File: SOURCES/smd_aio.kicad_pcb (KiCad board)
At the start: 2 copper layers, 159.8 x 99.8 mm, 225 parts, among them J1 RCA_01, J2 RCA_01, J3 RCA_01, J4 RCA_01, J5 Conn_01x02, J6 Conn_01x02, P1 MUTE, P10 CONN_01X02, P11 FCR684205T, P12 FCR684205R, P13 CONN_01X02, P14 CONN_01X02, P15 CONN_01X02, P16 TST, P17 MC4, P18 TST, P19 TST, P2 CONN_01X04, P20 TST, P21 TST, P22 TST, P23 TST, P24 MP11, P25 MP6, P26 MP10, P27 TST, P28 TST, P29 TST, P3 CONN_01X03, P30 TST, P31 CONN_01X03, P32 /SD, P33 GP4, P34 GP5, P35 GP6, P4 CONN_02X05 Boxed, P5 STDCONN, P6 CONN_02X04, P7 CONN_02X04, P8 CONN_02X04, P9 CONN_01X02, SW1 SW_PUSH, T1 Transformer_1P_1S_DA101JC, T2 Transformer_1P_1S_DA101JC, U1 ADAU1701, U10 IDT2309NZ, U11 LM1117MP-1.8, U12 LM1117MP-3.3, U13 OP279, U2 24AA256SN, U3 SN74LVC14ADG4, U4 TAS5760MDCAR, U5 CS8422-CNZ, U6 CS8406-CZZ, U7 LM2842Y, U8 MCP23008-xSS, U9 TAS5760MDCAR, X1 ASV-24.576MHz-EJ-T

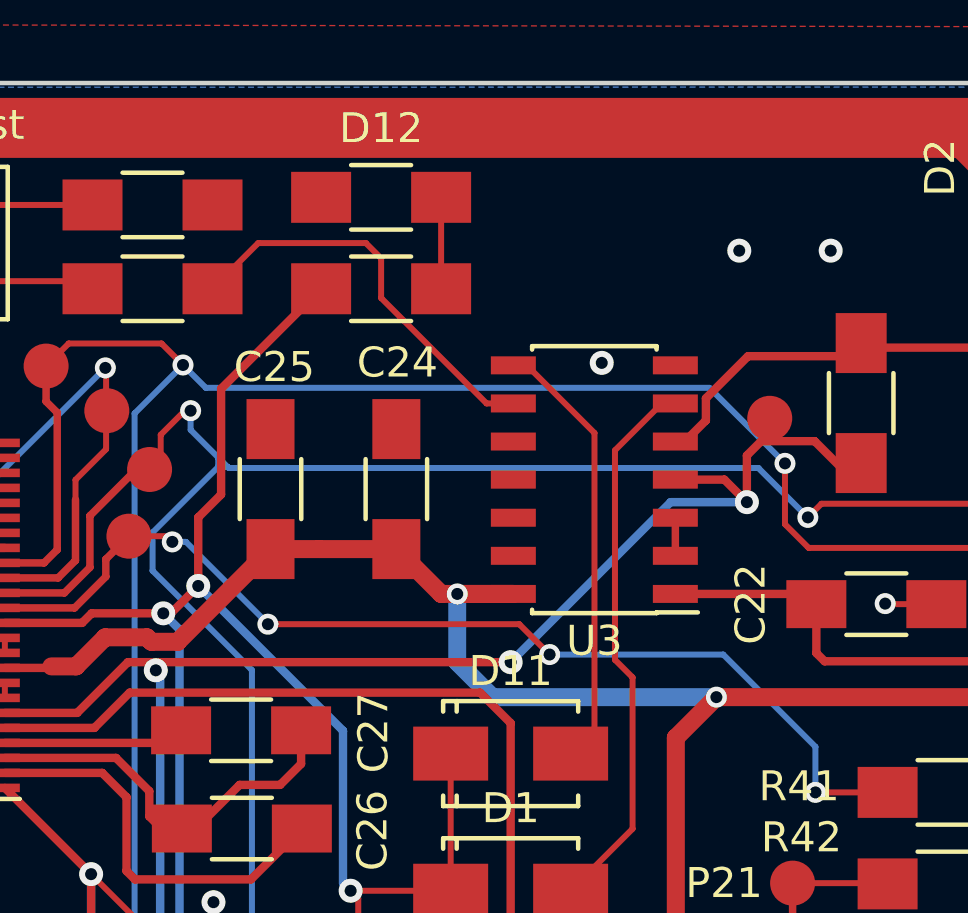
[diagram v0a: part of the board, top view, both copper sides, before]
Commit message: Added BAT54s OV protect.
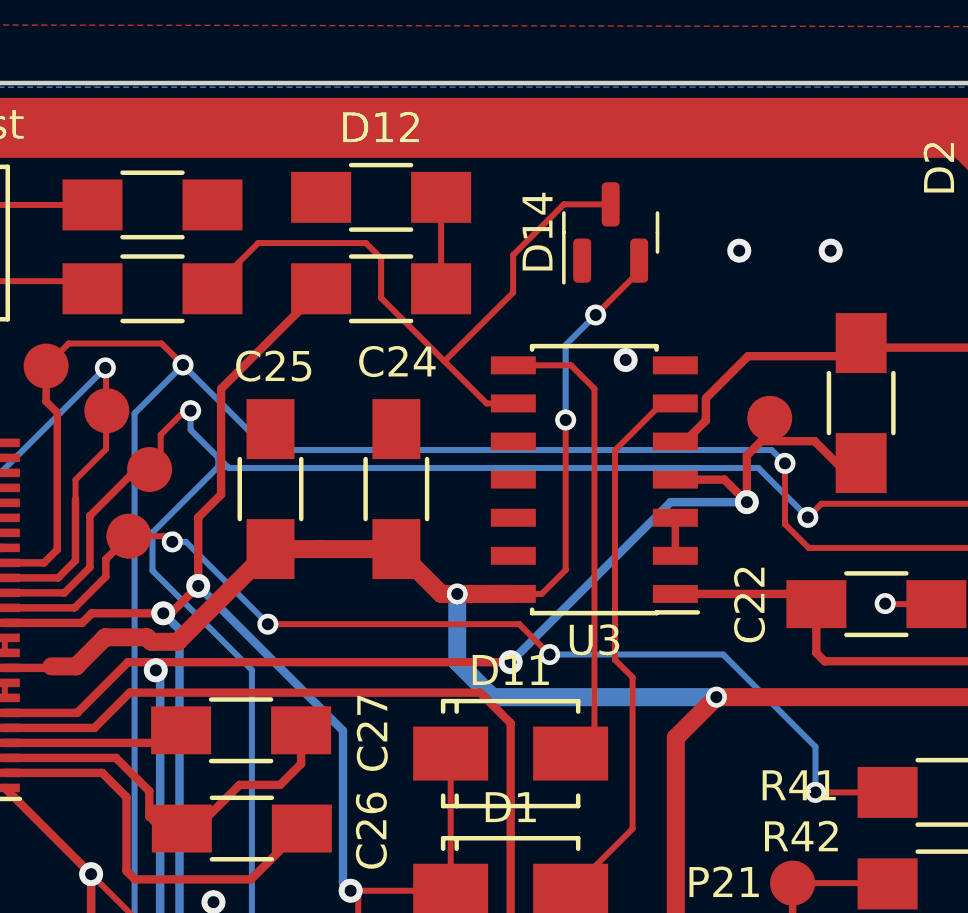
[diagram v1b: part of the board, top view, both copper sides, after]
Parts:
- added D14: BAT54S, Package_TO_SOT_SMD:SOT-23, F.Cu at (100.9, 22.0)
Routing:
- net +3V3: track 605.3 -> 618.7 mm, vias 14 -> 16
- net Net-(D14-COM): track 13.6 -> 22.1 mm
- net Net-(D11-A): track 14.7 -> 15.5 mm

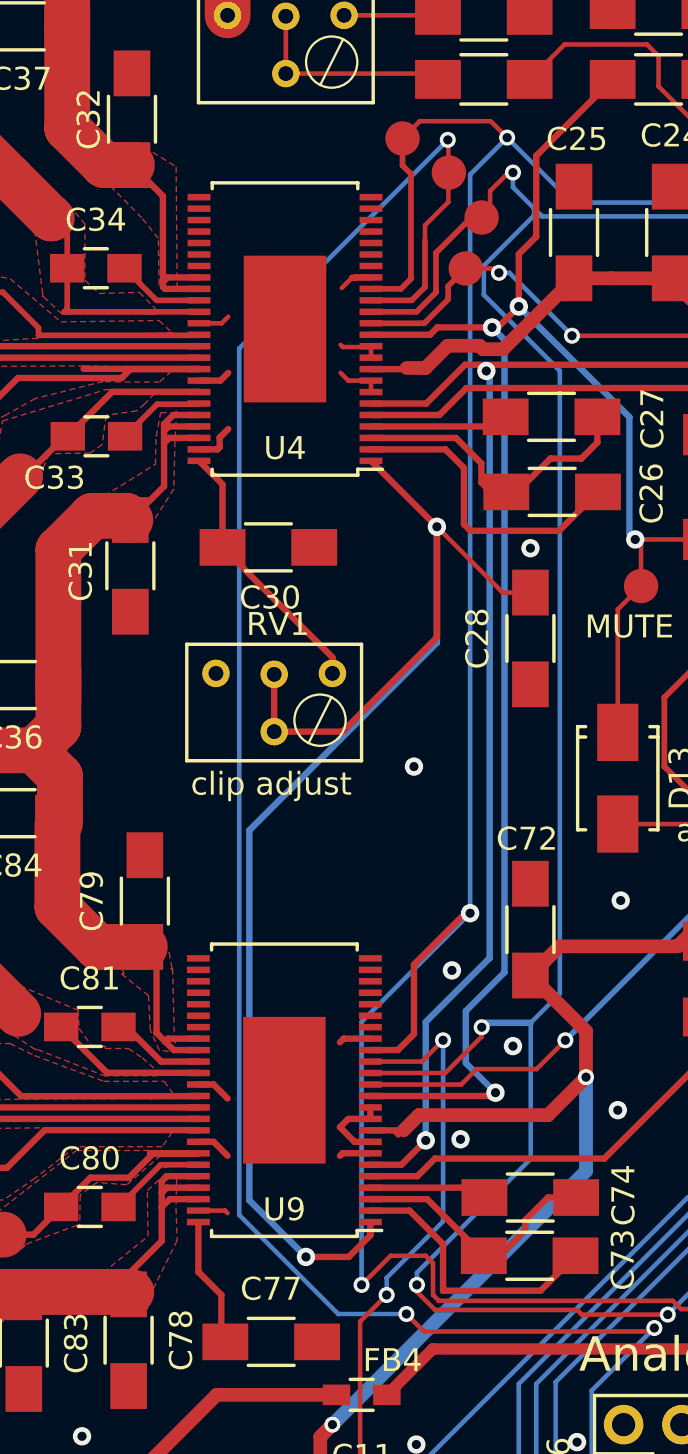
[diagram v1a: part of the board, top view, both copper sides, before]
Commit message: Cleaned up ground plane under amps.
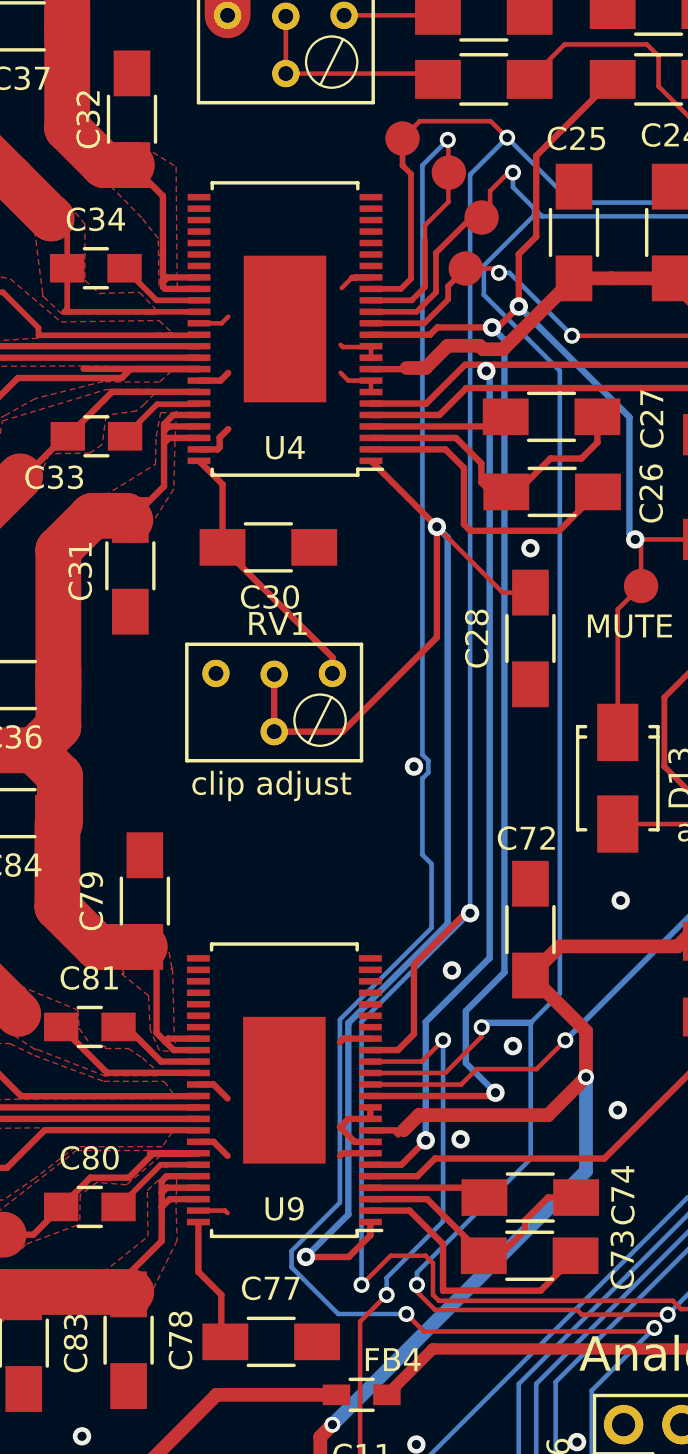
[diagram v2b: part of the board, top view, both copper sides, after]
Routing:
- net SFT_CLIP: track 65.5 -> 63.8 mm
- net MP6: track 110.7 -> 109.4 mm

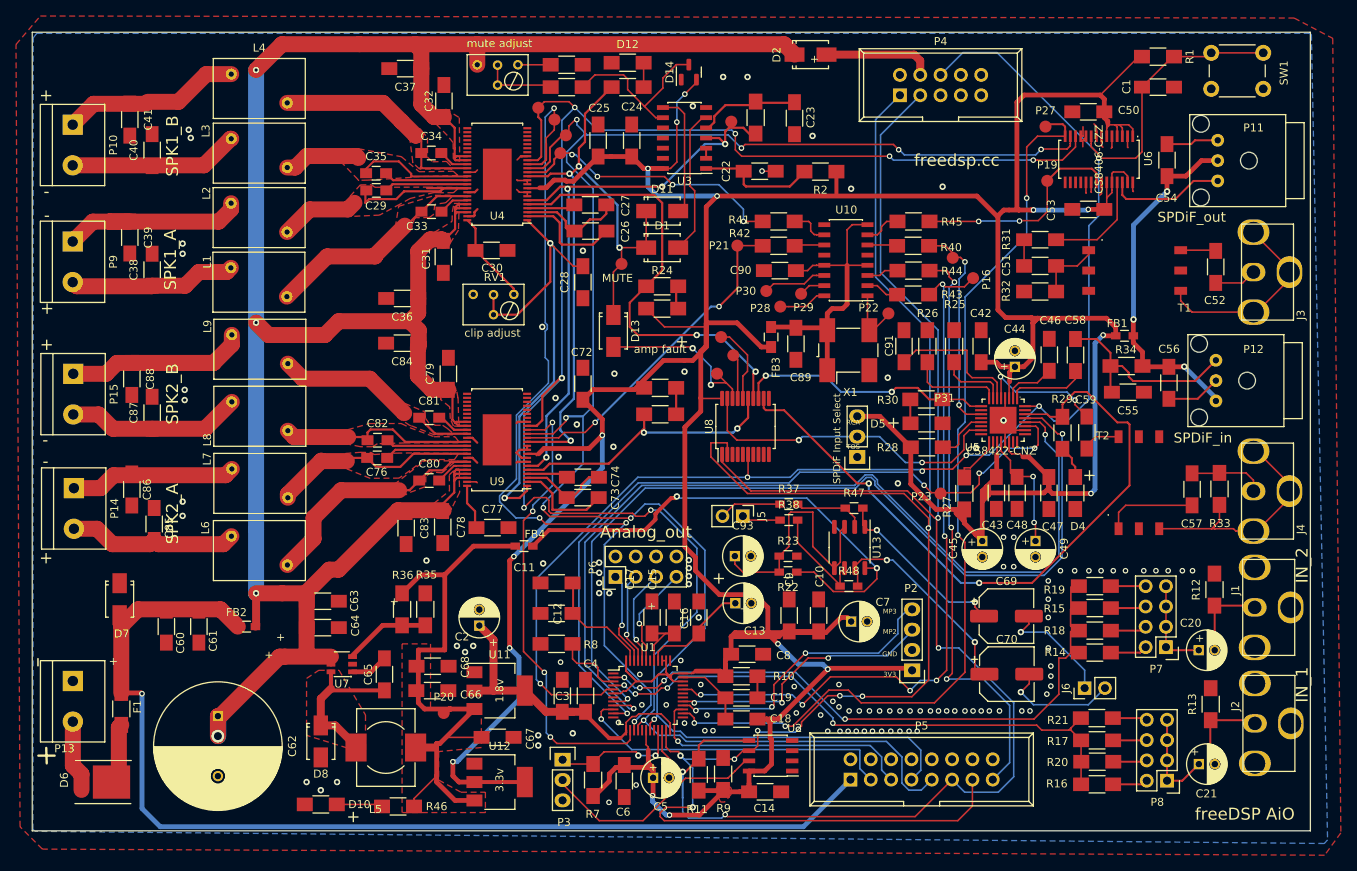
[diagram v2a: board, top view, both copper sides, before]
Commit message: Fixed Vin/Vcc issue.
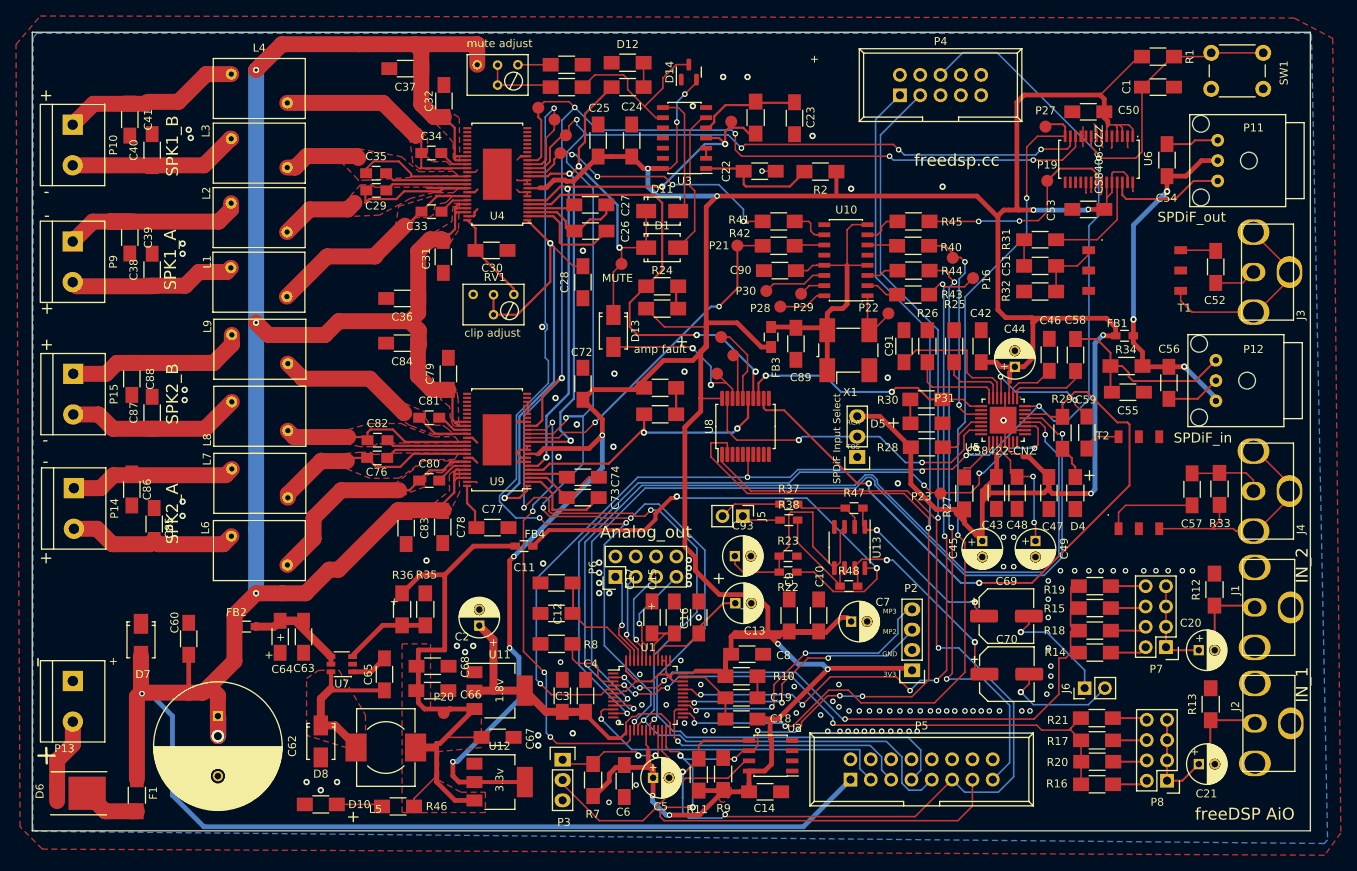
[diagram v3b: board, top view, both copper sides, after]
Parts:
- removed C61: 10u, fdsp_capacitor:C_1206_HandSoldering
- removed D2: B150, fdsp_diode:SMA
- moved F1 11.0 mm to (31.9, 112.4)
- moved D7 5.74 mm to (32.4, 93.0)
- moved C64 5.46 mm to (49.8, 92.6), turned to -90 degrees
- moved C63 5.06 mm to (52.7, 92.6), turned to -90 degrees
- moved D6 3.35 mm to (25.7, 112.1)
- moved C60 3.18 mm to (38.4, 92.8), turned to 90 degrees
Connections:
- C31 pad 1: VCC -> VIN
- C32 pad 1: VCC -> VIN
- C36 pad 1: VCC -> VIN
- C37 pad 1: VCC -> VIN
- C62 pad 1: VCC -> VIN
- C78 pad 1: VCC -> VIN
- C79 pad 1: VCC -> VIN
- C83 pad 1: VCC -> VIN
- C84 pad 1: VCC -> VIN
- RV2 pad 3: VCC -> VIN
- U4 pad 32: VCC -> VIN
- U4 pad 33: VCC -> VIN
- U4 pad 44: VCC -> VIN
- U4 pad 45: VCC -> VIN
- U4 pad 46: VCC -> VIN
- U9 pad 32: VCC -> VIN
- U9 pad 33: VCC -> VIN
- U9 pad 44: VCC -> VIN
- U9 pad 45: VCC -> VIN
- U9 pad 46: VCC -> VIN
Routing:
- net VCC: track 293.7 -> 15.6 mm, vias 4 -> 0
- net VIN: track 133.6 -> 375.7 mm, vias 1 -> 5
- net Net-(P4-P4): track 13.8 -> 0.00 mm
- net +12V: track 8.99 -> 10.8 mm

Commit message: Improved power traces.
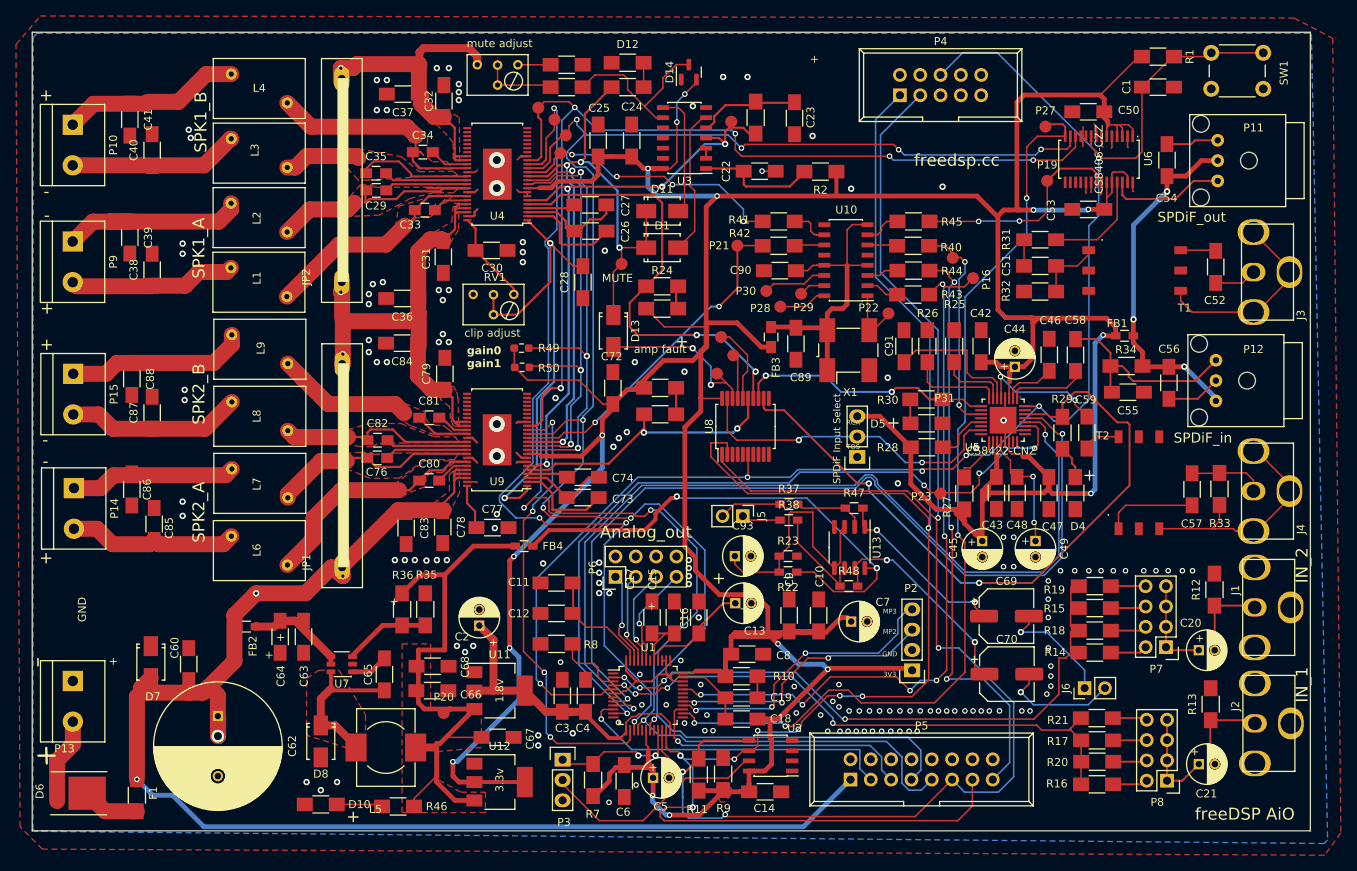
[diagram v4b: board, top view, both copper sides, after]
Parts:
- added JP1: Jumper_2_Bridged, JumperWires:Jumper-Wire_25mm_Blue, F.Cu at (57.5, 83.9)
- added JP2: Jumper_2_Bridged, JumperWires:Jumper-Wire_25mm_Blue, F.Cu at (57.5, 48.2)
- added R49: 1k, Resistor_SMD:R_0603_1608Metric_Pad0.98x0.95mm_HandSolder, F.Cu at (80.0, 56.5)
- added R50: 1k, Resistor_SMD:R_0603_1608Metric_Pad0.98x0.95mm_HandSolder, F.Cu at (80.0, 58.9)
- moved C72 3.78 mm to (91.4, 61.5)
- moved C37 3.20 mm to (65.1, 24.8)
- moved C60 3.16 mm to (38.4, 96.0)
- moved D7 3.05 mm to (33.6, 95.8)
- moved C34 1.06 mm to (67.6, 32.0)
- moved C33 0.85 mm to (67.9, 39.2)
- moved C79 0.44 mm to (70.4, 59.7)
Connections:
- C31 pad 1: VIN -> VIN1
- C32 pad 1: VIN -> VIN2
- C36 pad 1: VIN -> VIN1
- C37 pad 1: VIN -> VIN2
- C79 pad 1: VIN -> VIN1
- C84 pad 1: VIN -> VIN1
- RV2 pad 3: VIN -> VIN2
- U4 pad 10: GND -> SPK_GAIN0
- U4 pad 11: GND -> SPK_GAIN1
- U4 pad 32: VIN -> VIN2
- U4 pad 33: VIN -> VIN2
- U4 pad 44: VIN -> VIN1
- U4 pad 45: VIN -> VIN1
- U4 pad 46: VIN -> VIN1
- U9 pad 10: GND -> SPK_GAIN0
- U9 pad 11: GND -> SPK_GAIN1
- U9 pad 32: VIN -> VIN1
- U9 pad 33: VIN -> VIN1
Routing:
- net VIN: track 375.7 -> 181.9 mm, vias 5 -> 4
- net VIN1: track 0.00 -> 59.6 mm, vias 0 -> 2
- net SPK_GAIN0: track 0.00 -> 56.7 mm, vias 0 -> 3
- net SPK_GAIN1: track 0.00 -> 53.6 mm, vias 0 -> 3
- net VIN2: track 0.00 -> 42.8 mm, vias 0 -> 1
- net +3V3: track 618.7 -> 631.9 mm
- net GND: track 58.4 -> 54.5 mm, vias 125 -> 161
- net /AMPx2_1/SPK_OUTB+: track 28.5 -> 29.7 mm
- net Net-(U4-BSTRPB+): track 3.83 -> 4.93 mm
- net MP11: track 225.0 -> 225.8 mm
- net Net-(U4-BSTRPA+): track 3.82 -> 4.57 mm
- net SPK_SD: track 74.3 -> 74.9 mm
- added copper zone on F.Cu, net VIN
- removed copper zone on F.Cu, net VCC
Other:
- board text added: "gain0 gain1"

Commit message: Minor improvents
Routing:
- net BRD_RST: track 199.2 -> 200.6 mm
- net SFT_CLIP: track 63.8 -> 62.8 mm
- net VIN1: track 59.6 -> 60.6 mm
- net GND: track 54.5 -> 55.5 mm, vias 161 -> 197
- net MP6: track 109.4 -> 108.5 mm
- net VIN: track 181.9 -> 181.1 mm
